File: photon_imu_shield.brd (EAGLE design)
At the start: 35.6 x 35.6 mm, 30 parts, among them U1 LSM9DS1

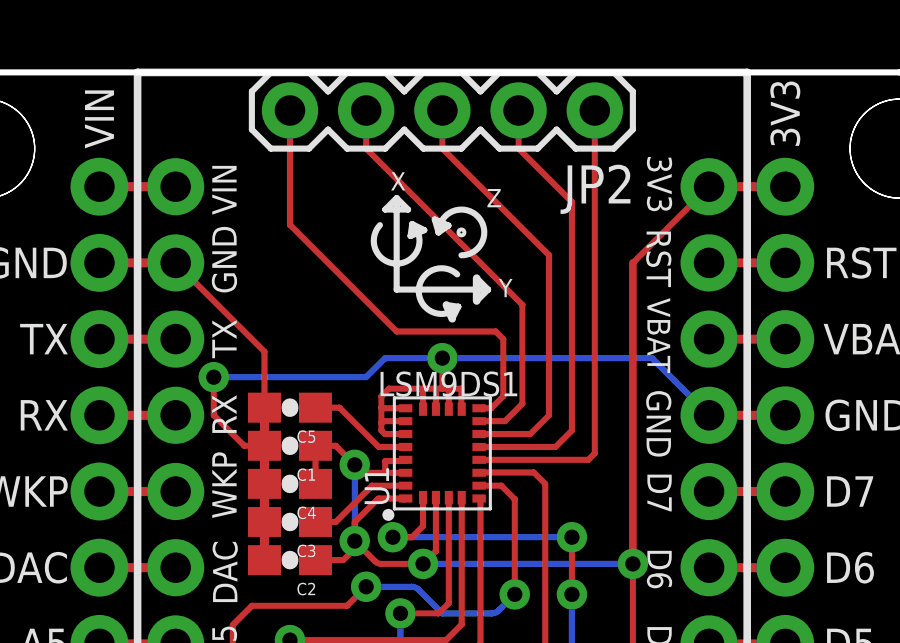
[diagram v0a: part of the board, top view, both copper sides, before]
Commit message: Improved trace spacing
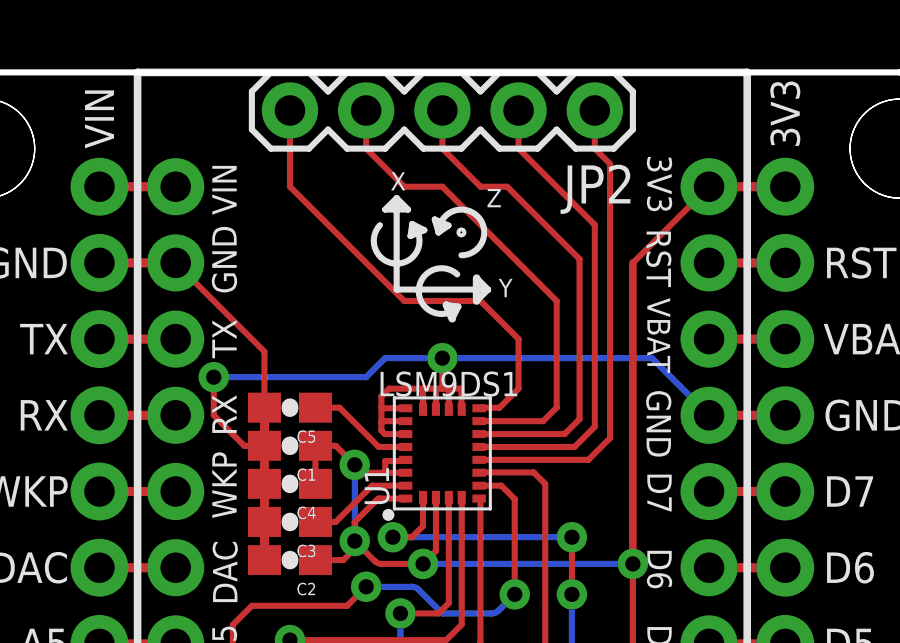
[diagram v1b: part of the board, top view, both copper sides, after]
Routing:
- net INT2_A/G: track 13.6 -> 16.1 mm
- net INT1_A/G: track 14.2 -> 16.3 mm
- net INT_M: track 14.7 -> 15.7 mm
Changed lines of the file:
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@@
 <layer number="47" name="Measures" color="7" fill="1" visible="no" active="yes"/>
 <layer number="48" name="Document" color="7" fill="1" visible="no" active="yes"/>
-<layer number="49" name="Reference" color="7" fill="1" visible="yes" active="yes"/>
+<layer number="49" name="Reference" color="7" fill="1" visible="no" active="yes"/>
 <layer number="50" name="dxf" color="7" fill="1" visible="no" active="no"/>
 <layer number="51" name="tDocu" color="6" fill="1" visible="yes" active="yes"/>
@@
 <contactref element="U1" pad="11"/>
 <contactref element="JP2" pad="3"/>
-<wire x1="20.711" y1="23.505" x2="19.005" y2="23.505" width="0.2032" layer="1"/>
+<wire x1="21.854" y1="23.505" x2="19.005" y2="23.505" width="0.2032" layer="1"/>
 <wire x1="17.78" y1="34.29" x2="17.78" y2="33.02" width="0.2032" layer="1"/>
-<wire x1="17.78" y1="33.02" x2="21.336" y2="29.464" width="0.2032" layer="1"/>
-<wire x1="20.711" y1="23.505" x2="21.336" y2="24.13" width="0.2032" layer="1"/>
-<wire x1="21.336" y1="24.13" x2="21.336" y2="29.464" width="0.2032" layer="1"/>
+<wire x1="21.854" y1="23.505" x2="22.352" y2="24.003" width="0.2032" layer="1"/>
+<wire x1="22.352" y1="24.003" x2="22.352" y2="29.337" width="0.2032" layer="1"/>
+<wire x1="22.352" y1="29.337" x2="19.939" y2="31.75" width="0.2032" layer="1"/>
+<wire x1="19.939" y1="31.75" x2="19.05" y2="31.75" width="0.2032" layer="1"/>
+<wire x1="19.05" y1="31.75" x2="17.78" y2="33.02" width="0.2032" layer="1"/>
 </signal>
 <signal name="INT2_A/G">
 <contactref element="U1" pad="12"/>
 <contactref element="JP2" pad="4"/>
-<wire x1="20.447" y1="27.813" x2="20.447" y2="24.511" width="0.2032" layer="1"/>
-<wire x1="20.447" y1="24.511" x2="19.871" y2="23.935" width="0.2032" layer="1"/>
-<wire x1="19.871" y1="23.935" x2="19.005" y2="23.935" width="0.2032" layer="1"/>
+<wire x1="21.141" y1="23.935" x2="19.005" y2="23.935" width="0.2032" layer="1"/>
 <wire x1="15.24" y1="34.29" x2="15.24" y2="33.02" width="0.2032" layer="1"/>
-<wire x1="15.24" y1="33.02" x2="20.447" y2="27.813" width="0.2032" layer="1"/>
+<wire x1="21.141" y1="23.935" x2="21.59" y2="24.384" width="0.2032" layer="1"/>
+<wire x1="21.59" y1="24.384" x2="21.59" y2="27.94" width="0.2032" layer="1"/>
+<wire x1="21.59" y1="27.94" x2="17.78" y2="31.75" width="0.2032" layer="1"/>
+<wire x1="17.78" y1="31.75" x2="16.51" y2="31.75" width="0.2032" layer="1"/>
+<wire x1="16.51" y1="31.75" x2="15.24" y2="33.02" width="0.2032" layer="1"/>
 </signal>
 <signal name="DEN_A/G">
 <contactref element="U1" pad="13"/>
 <contactref element="JP2" pad="5"/>
-<wire x1="12.7" y1="34.29" x2="12.7" y2="30.48" width="0.2032" layer="1"/>
-<wire x1="19.558" y1="26.924" x2="19.812" y2="26.67" width="0.2032" layer="1"/>
-<wire x1="19.812" y1="26.67" x2="19.812" y2="24.765" width="0.2032" layer="1"/>
-<wire x1="19.812" y1="24.765" x2="19.412" y2="24.365" width="0.2032" layer="1"/>
-<wire x1="19.412" y1="24.365" x2="19.005" y2="24.365" width="0.2032" layer="1"/>
-<wire x1="19.558" y1="26.924" x2="16.256" y2="26.924" width="0.2032" layer="1"/>
-<wire x1="16.256" y1="26.924" x2="12.7" y2="30.48" width="0.2032" layer="1"/>
+<wire x1="19.005" y1="24.365" x2="19.024" y2="24.384" width="0.2032" layer="1"/>
+<wire x1="19.024" y1="24.384" x2="19.685" y2="24.384" width="0.2032" layer="1"/>
+<wire x1="19.685" y1="24.384" x2="20.32" y2="25.019" width="0.2032" layer="1"/>
+<wire x1="20.32" y1="25.019" x2="20.32" y2="26.67" width="0.2032" layer="1"/>
+<wire x1="20.32" y1="26.67" x2="19.05" y2="27.94" width="0.2032" layer="1"/>
+<wire x1="19.05" y1="27.94" x2="16.51" y2="27.94" width="0.2032" layer="1"/>
+<wire x1="16.51" y1="27.94" x2="12.7" y2="31.75" width="0.2032" layer="1"/>
+<wire x1="12.7" y1="31.75" x2="12.7" y2="34.29" width="0.2032" layer="1"/>
 </signal>
 <signal name="DRDY_M">
@@
 <contactref element="JP2" pad="1"/>
 <wire x1="19.005" y1="22.645" x2="22.645" y2="22.645" width="0.2032" layer="1"/>
-<wire x1="22.645" y1="22.645" x2="22.86" y2="22.86" width="0.2032" layer="1"/>
-<wire x1="22.86" y1="22.86" x2="22.86" y2="34.29" width="0.2032" layer="1"/>
+<wire x1="22.645" y1="22.645" x2="23.368" y2="23.368" width="0.2032" layer="1"/>
+<wire x1="23.368" y1="23.368" x2="23.368" y2="32.512" width="0.2032" layer="1"/>
+<wire x1="23.368" y1="32.512" x2="22.86" y2="33.02" width="0.2032" layer="1"/>
+<wire x1="22.86" y1="33.02" x2="22.86" y2="34.29" width="0.2032" layer="1"/>
 </signal>
 <signal name="INT_M">
 <contactref element="U1" pad="10"/>
 <contactref element="JP2" pad="2"/>
-<wire x1="21.551" y1="23.075" x2="19.005" y2="23.075" width="0.2032" layer="1"/>
+<wire x1="22.186" y1="23.075" x2="19.005" y2="23.075" width="0.2032" layer="1"/>
 <wire x1="20.32" y1="34.29" x2="20.32" y2="33.02" width="0.2032" layer="1"/>
-<wire x1="20.32" y1="33.02" x2="22.098" y2="31.242" width="0.2032" layer="1"/>
-<wire x1="21.551" y1="23.075" x2="22.098" y2="23.622" width="0.2032" layer="1"/>
-<wire x1="22.098" y1="23.622" x2="22.098" y2="31.242" width="0.2032" layer="1"/>
+<wire x1="22.186" y1="23.075" x2="22.86" y2="23.749" width="0.2032" layer="1"/>
+<wire x1="22.86" y1="23.749" x2="22.86" y2="30.48" width="0.2032" layer="1"/>
+<wire x1="22.86" y1="30.48" x2="20.32" y2="33.02" width="0.2032" layer="1"/>
 </signal>
 </signals>

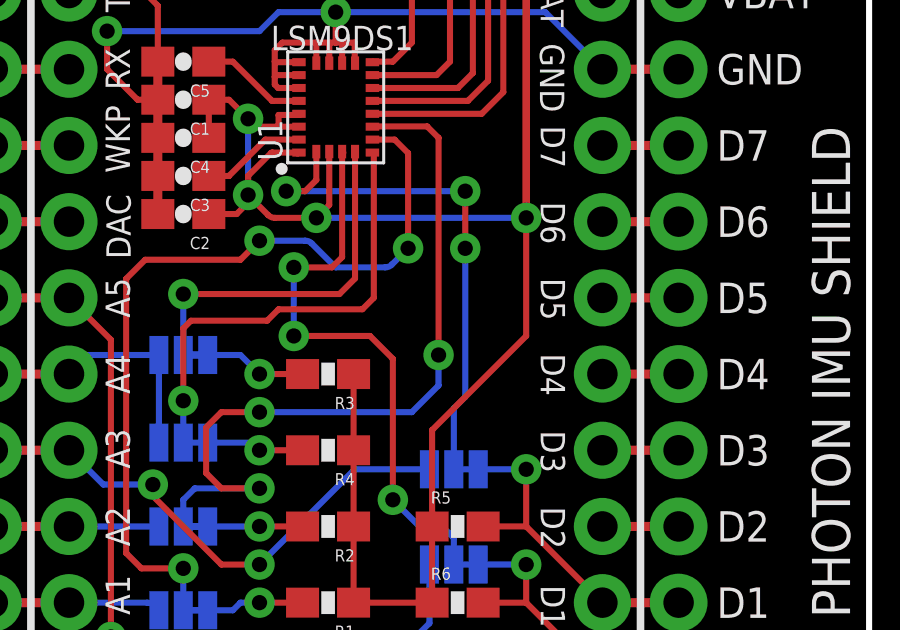
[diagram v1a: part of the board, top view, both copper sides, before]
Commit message: Fixed silk, added switch vias
Not adding JST, b/c pins are adjacent so can just solder to them.
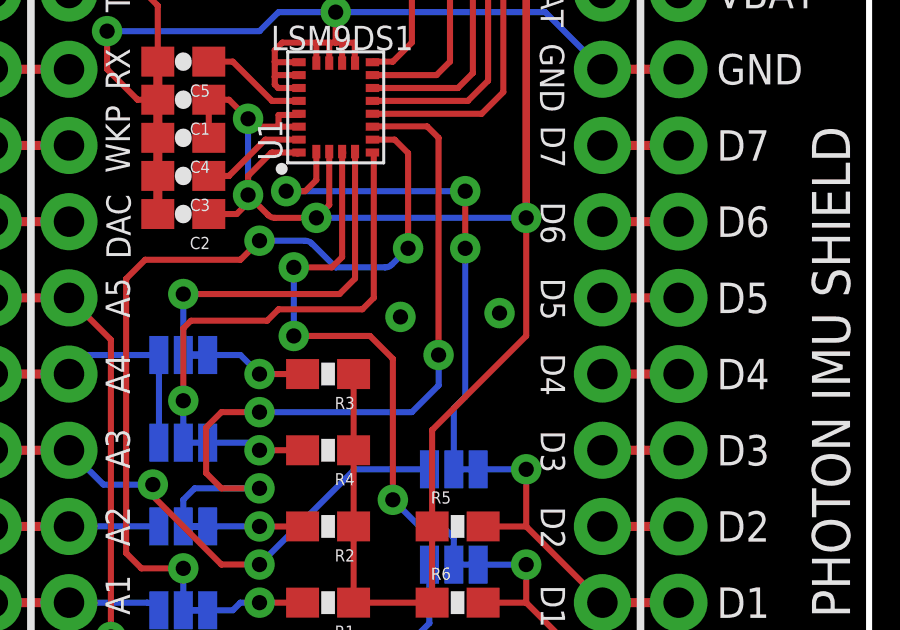
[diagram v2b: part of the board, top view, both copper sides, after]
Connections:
- new net VBAT: JP1.22, JP1.VBAT
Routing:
- net GND: vias 2 -> 4
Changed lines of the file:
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@@
 <grid distance="0.05" unitdist="inch" unit="inch" style="lines" multiple="1" display="yes" altdistance="0.005" altunitdist="inch" altunit="inch"/>
 <layers>
-<layer number="1" name="Top" color="4" fill="1" visible="yes" active="yes"/>
+<layer number="1" name="Top" color="4" fill="1" visible="no" active="yes"/>
 <layer number="2" name="Route2" color="1" fill="3" visible="no" active="no"/>
 <layer number="3" name="Route3" color="4" fill="3" visible="no" active="no"/>
@@
 <layer number="14" name="Route14" color="1" fill="6" visible="no" active="no"/>
 <layer number="15" name="Route15" color="4" fill="6" visible="no" active="no"/>
-<layer number="16" name="Bottom" color="1" fill="1" visible="yes" active="yes"/>
+<layer number="16" name="Bottom" color="1" fill="1" visible="no" active="yes"/>
 <layer number="17" name="Pads" color="2" fill="1" visible="yes" active="yes"/>
 <layer number="18" name="Vias" color="2" fill="1" visible="yes" active="yes"/>
-<layer number="19" name="Unrouted" color="6" fill="1" visible="yes" active="yes"/>
-<layer number="20" name="Dimension" color="15" fill="1" visible="yes" active="yes"/>
-<layer number="21" name="tPlace" color="16" fill="1" visible="yes" active="yes"/>
+<layer number="19" name="Unrouted" color="6" fill="1" visible="no" active="yes"/>
+<layer number="20" name="Dimension" color="15" fill="1" visible="no" active="yes"/>
+<layer number="21" name="tPlace" color="16" fill="1" visible="no" active="yes"/>
 <layer number="22" name="bPlace" color="14" fill="1" visible="yes" active="yes"/>
-<layer number="23" name="tOrigins" color="15" fill="1" visible="yes" active="yes"/>
-<layer number="24" name="bOrigins" color="15" fill="1" visible="yes" active="yes"/>
+<layer number="23" name="tOrigins" color="15" fill="1" visible="no" active="yes"/>
+<layer number="24" name="bOrigins" color="15" fill="1" visible="no" active="yes"/>
 <layer number="25" name="tNames" color="7" fill="1" visible="no" active="yes"/>
 <layer number="26" name="bNames" color="7" fill="1" visible="no" active="yes"/>
@@
 <layer number="43" name="vRestrict" color="2" fill="10" visible="no" active="yes"/>
 <layer number="44" name="Drills" color="7" fill="1" visible="no" active="yes"/>
-<layer number="45" name="Holes" color="7" fill="1" visible="yes" active="yes"/>
+<layer number="45" name="Holes" color="7" fill="1" visible="no" active="yes"/>
 <layer number="46" name="Milling" color="3" fill="1" visible="no" active="yes"/>
 <layer number="47" name="Measures" color="7" fill="1" visible="no" active="yes"/>
@@
 <layer number="49" name="Reference" color="7" fill="1" visible="no" active="yes"/>
 <layer number="50" name="dxf" color="7" fill="1" visible="no" active="no"/>
-<layer number="51" name="tDocu" color="6" fill="1" visible="yes" active="yes"/>
+<layer number="51" name="tDocu" color="6" fill="1" visible="no" active="yes"/>
 <layer number="52" name="bDocu" color="7" fill="1" visible="no" active="yes"/>
 <layer number="53" name="tGND_GNDA" color="7" fill="9" visible="no" active="no"/>
@@
 <wire x1="0" y1="33.02" x2="2.54" y2="35.56" width="0.2032" layer="20" curve="-90"/>
 <text x="14.351" y="-40.767" size="1.778" layer="51" ratio="15">Ben Leduc-Mills</text>
-<text x="12.319" y="30.734" size="0.8128" layer="22" font="vector" ratio="12" rot="MR0" align="bottom-center">DEN
+<text x="11.303" y="31.623" size="0.8128" layer="22" font="vector" ratio="12" rot="MR90" align="bottom-center">DEN
 AG</text>
-<text x="14.986" y="30.734" size="0.8128" layer="22" font="vector" ratio="12" rot="MR0" align="bottom-center">INT2
+<text x="15.875" y="31.496" size="0.8128" layer="22" font="vector" ratio="12" rot="MR270" align="bottom-center">INT2
 AG</text>
-<text x="18.034" y="30.734" size="0.8128" layer="22" font="vector" ratio="12" rot="MR0" align="bottom-center">INT1
+<text x="18.669" y="31.623" size="0.8128" layer="22" font="vector" ratio="12" rot="MR270" align="bottom-center">INT1
 AG</text>
-<text x="20.574" y="30.734" size="0.8128" layer="22" font="vector" ratio="12" rot="MR0" align="bottom-center">INT
+<text x="21.209" y="31.623" size="0.8128" layer="22" font="vector" ratio="12" rot="MR270" align="bottom-center">INT
 M</text>
-<text x="23.114" y="30.734" size="0.8128" layer="22" font="vector" ratio="12" rot="MR0" align="bottom-center">DRDY
+<text x="23.876" y="31.623" size="0.8128" layer="22" font="vector" ratio="12" rot="MR270" align="bottom-center">DRDY
 M</text>
 </plain>
@@
 <wire x1="26.67" y1="24.13" x2="24.765" y2="26.035" width="0.2032" layer="16"/>
 <wire x1="24.765" y1="26.035" x2="17.78" y2="26.035" width="0.2032" layer="16"/>
+<via x="23.241" y="16.002" extent="1-16" drill="0.508"/>
+<via x="19.939" y="15.875" extent="1-16" drill="0.508"/>
 </signal>
 <signal name="VDD">
@@
 <wire x1="22.86" y1="30.48" x2="20.32" y2="33.02" width="0.2032" layer="1"/>
 </signal>
+<signal name="VBAT">
+<contactref element="JP1" pad="22"/>
+<contactref element="JP1" pad="VBAT"/>
+</signal>
 </signals>

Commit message: QC fixes
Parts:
- moved FID2 3.81 mm to (1.27, 4.95)
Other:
- board text added: "Board Measurements: 1.4in x 1.4in"
- board text removed: "LSM9DS1"
